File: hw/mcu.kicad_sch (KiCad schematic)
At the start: 22 parts, among them J301 SWD/JTAG, Q301 60V logic-level N-ch, U301 S32K148_144LQFP, U302 TPS3850G33

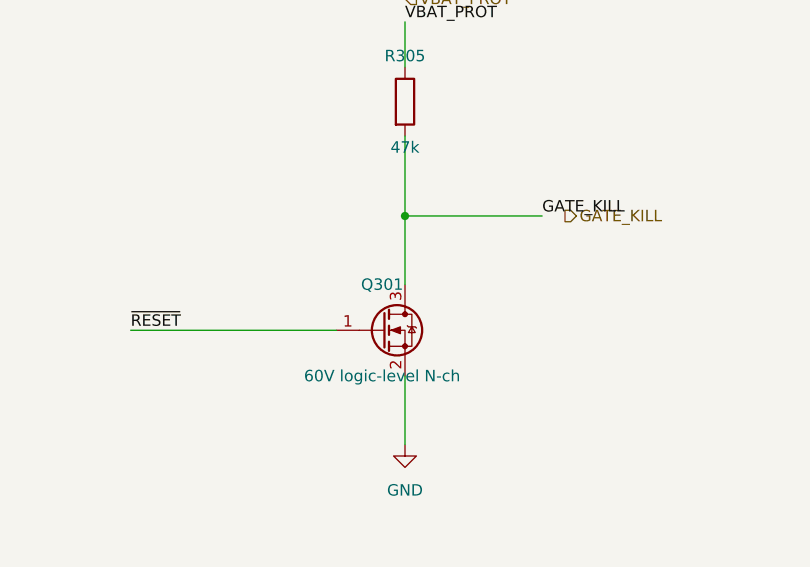
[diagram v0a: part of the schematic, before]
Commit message: Clamp GATE_KILL at 12 V and buffer the relay gates to 5 V
Choosing the small-signal FETs found two gate-drive errors.

GATE_KILL is pulled to VBAT_PROT so the kill path survives a 3V3
brownout, but only FET gates load it, so it followed the rail to
73.3 V on pulse 2a -- 3.7x a +/-20 V Vgs rating. A BZX84-C12-Q now
holds it at 12.7 V (13.7 V hot); transient_clamp checks the margin,
the zener current and the pullup dissipation.

The relay FETs were driven straight from 3.3 V GPIOs, with a note
claiming full enhancement at 3.0 V. No 100 V automotive small-signal
FET checked (PMV280ENEA, DMN10H220LQ, BSS123N) is specified below
Vgs = 4.5 V. An SN74AHCT1G125-Q1 on 5V_MAIN now drives each gate,
with a 100k input pulldown for reset; relay_driver checks overdrive
and drop.

Parts: 2N7002BK for the nine kill FETs and the reset inverter,
PMV280ENEA for the relay FETs. Also fixes the diagonal VBAT_PROT wire
to both relay flyback diodes.

24/24 sim blocks, netlist gate passing, 43 of 297 parts with footprints.
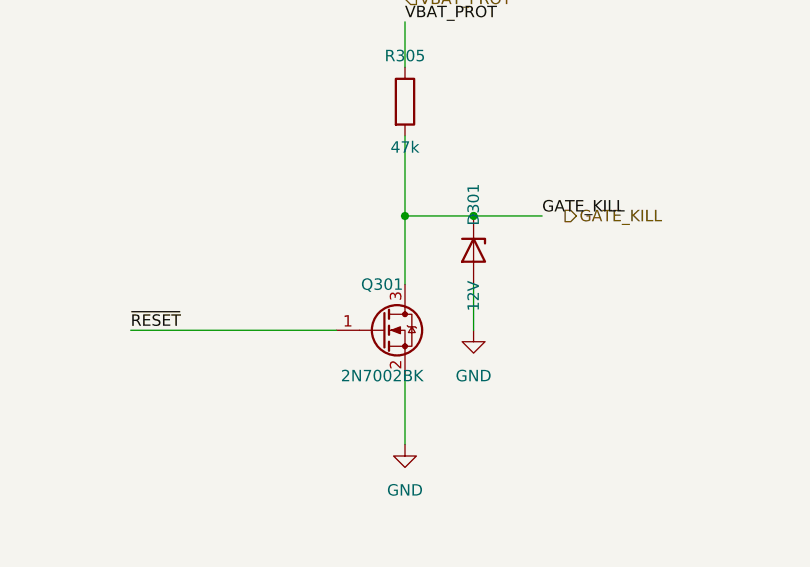
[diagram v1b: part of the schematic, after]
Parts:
- added D301: 12V, Package_TO_SOT_SMD:SOT-23, symbol Device:D_Zener
- Q301: value 60V logic-level N-ch -> 2N7002BK; footprint (none) -> Package_TO_SOT_SMD:SOT-23; MPN (none) -> 2N7002BK; Vgs (none) -> Gate from ~RESET at 3.3 V: Vth 1.1-2.1 V, and it sinks 1.6 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
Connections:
- net GATE_KILL: now also D301.1 (K)
- net GND: now also D301.2 (A)
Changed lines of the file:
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@@
       (effects (font (size 1.27 1.27)))
     )
-    (property "Value" "60V logic-level N-ch" (id 1) (at 295 345.08 0)
-      (effects (font (size 1.27 1.27)))
-    )
-    (property "Footprint" "" (id 2) (at 295 340 0)
+    (property "Value" "2N7002BK" (id 1) (at 295 345.08 0)
+      (effects (font (size 1.27 1.27)))
+    )
+    (property "Footprint" "Package_TO_SOT_SMD:SOT-23" (id 2) (at 295 340 0)
       (effects (font (size 1.27 1.27)) hide)
     )
@@
       (effects (font (size 1.27 1.27)) hide)
     )
-    (property "Source" "memo 11 Recommendation -- 'through one inverting stage'; supervisor.cir models the inverter and kill FET as one switch" (id 4) (at 295 340 0)
-      (effects (font (size 1.27 1.27)) hide)
-    )
-    (property "Note" "RESET low (fault) turns this OFF, so the pullup asserts GATE_KILL high" (id 5) (at 295 340 0)
+    (property "MPN" "2N7002BK" (id 4) (at 295 340 0)
+      (effects (font (size 1.27 1.27)) hide)
+    )
+    (property "Vgs" "Gate from ~RESET at 3.3 V: Vth 1.1-2.1 V, and it sinks 1.6 mA at most (73.3 V / 47k)" (id 5) (at 295 340 0)
+      (effects (font (size 1.27 1.27)) hide)
+    )
+    (property "Source" "memo 11 Recommendation -- 'through one inverting stage'; supervisor.cir models the inverter and kill FET as one switch" (id 6) (at 295 340 0)
+      (effects (font (size 1.27 1.27)) hide)
+    )
+    (property "Note" "RESET low (fault) turns this OFF, so the pullup asserts GATE_KILL high" (id 7) (at 295 340 0)
       (effects (font (size 1.27 1.27)) hide)
     )
@@
     (stroke (width 0) (type default))
   )
-  (wire (pts (xy 297.54 327.3) (xy 312.78 327.3))
-    (stroke (width 0) (type default))
+  (symbol (lib_id "Device:D_Zener") (at 305.16 331.11 270) (unit 1)
+    (in_bom yes) (on_board yes) (fields_autoplaced)
+    (property "Reference" "D301" (id 0) (at 305.16 326.03000000000003 0)
+      (effects (font (size 1.27 1.27)))
+    )
+    (property "Value" "12V" (id 1) (at 305.16 336.19 0)
+      (effects (font (size 1.27 1.27)))
+    )
+    (property "Footprint" "Package_TO_SOT_SMD:SOT-23" (id 2) (at 305.16 331.11 0)
+      (effects (font (size 1.27 1.27)) hide)
+    )
+    (property "Datasheet" "~" (id 3) (at 305.16 331.11 0)
+      (effects (font (size 1.27 1.27)) hide)
+    )
+    (property "MPN" "BZX84-C12-Q" (id 4) (at 305.16 331.11 0)
+      (effects (font (size 1.27 1.27)) hide)
+    )
+    (property "Source" "run_sim transient_clamp -- GATE_KILL clamp" (id 5) (at 305.16 331.11 0)
+      (effects (font (size 1.27 1.27)) hide)
+    )
+    (property "Note" "Cathode GATE_KILL, anode GND: kill gates never exceed 12.7 V against a 20 V Vgs rating, whatever VBAT_PROT does" (id 6) (at 305.16 331.11 0)
+      (effects (font (size 1.27 1.27)) hide)
+    )
+  )
+  (wire (pts (xy 297.54 327.3) (xy 305.16 327.3))
+    (stroke (width 0) (type default))
+  )
+  (wire (pts (xy 305.16 327.3) (xy 312.78 327.3))
+    (stroke (width 0) (type default))
+  )
+  (junction (at 305.16 327.3) (diameter 0) (color 0 0 0 0)
+  )
+  (wire (pts (xy 305.16 334.92) (xy 305.16 340.0))
+    (stroke (width 0) (type default))
+  )
+  (symbol (lib_id "power:GND") (at 305.16 340.0 0) (unit 1)
+    (in_bom yes) (on_board yes) (fields_autoplaced)
+    (property "Reference" "#PWR307" (id 0) (at 305.16 334.92 0)
+      (effects (font (size 1.27 1.27)) hide)
+    )
+    (property "Value" "GND" (id 1) (at 305.16 345.08 0)
+      (effects (font (size 1.27 1.27)))
+    )
+    (property "Footprint" "" (id 2) (at 305.16 340.0 0)
+      (effects (font (size 1.27 1.27)) hide)
+    )
+    (property "Datasheet" "~" (id 3) (at 305.16 340.0 0)
+      (effects (font (size 1.27 1.27)) hide)
+    )
   )
   (label "GATE_KILL" (at 312.78 327.3 0)
@@
   (symbol (lib_id "power:GND") (at 400.0 405.16 0) (unit 1)
     (in_bom yes) (on_board yes) (fields_autoplaced)
-    (property "Reference" "#PWR307" (id 0) (at 400.0 400.08000000000004 0)
+    (property "Reference" "#PWR308" (id 0) (at 400.0 400.08000000000004 0)
       (effects (font (size 1.27 1.27)) hide)
     )
@@
   (symbol (lib_id "power:GND") (at 267.92 405.16 0) (unit 1)
     (in_bom yes) (on_board yes) (fields_autoplaced)
-    (property "Reference" "#PWR308" (id 0) (at 267.92 400.08000000000004 0)
+    (property "Reference" "#PWR309" (id 0) (at 267.92 400.08000000000004 0)
       (effects (font (size 1.27 1.27)) hide)
     )
@@
   (symbol (lib_id "power:GND") (at 385.0 368.1 0) (unit 1)
     (in_bom yes) (on_board yes) (fields_autoplaced)
-    (property "Reference" "#PWR309" (id 0) (at 385 363.02000000000004 0)
-      (effects (font (size 1.27 1.27)) hide)
-    )
+    (property "Reference" "#PWR310" (id 0) (at 385 363.02000000000004 0)
+      (effects (font (size 1.27 1.27)) hide)
+    )

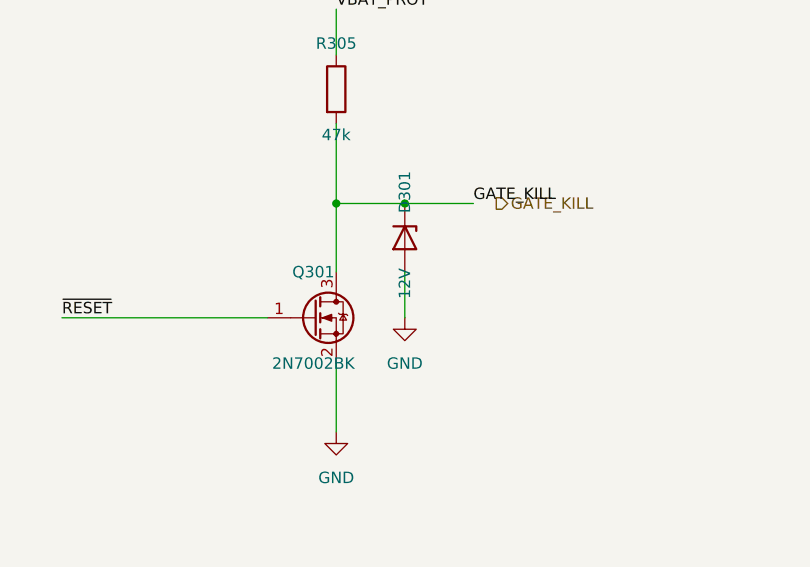
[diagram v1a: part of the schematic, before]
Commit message: Choose the diodes; the boost VDD clamp was 10 V over its pin rating
Part numbers for 27 diodes, each against a retrieved datasheet, applied
through one table (schlib.CHOSEN) keyed by symbol and class value, so
the class stays on the part as a field:
  VS-16EDH02HM3 x7   injector recirculation / blocking / freewheel
  VS-2EMH02HM3       boost diode
  VS-1EMH02HM3 x8    bootstrap and relay flyback
  VS-3ECH02HM3       metering freewheel
  SS20PH102HM3       negative-clamp backstop Schottky
  SMCJ43CA-HM3, SMAJ48CA-HE3, BZX84-C12-Q x2, BZX84-C13-Q, BZG03C36-HM3

The TPS40210 VDD clamp had been checked as an ideal 43.0 V source
behind 47 ohm. The real part in that class (40-46 V, +0.12 %/K, 45 ohm)
puts 61.9 V on a 52 V pin at 125 C, and its 40 V minimum conducts on
the load dump it was chosen to avoid. Now 220 ohm -- which the chosen
switch's gate charge allows -- and a 36 V zener: 46.6 V worst case with
tolerance, tempco and impedance, 33 mA on the dump. 39 V was tried
first; the transient_clamp rail table rejected it at 1.05x. The old
design stays as a pinned check.

TO-277A and SOT-23 zeners put the cathode on pad 3. gen_footprints.py
derives renumbered copies into lib/ecu25kva.pretty (new fp-lib-table).
The GATE_KILL zener, footprinted in the previous commit with the stock
SOT-23, had been reversed.

Left open as LOWV-CLAMP: the 15 zeners at 3.0 and 3.3 V. At tens of uA
a sub-5 V zener's knee is soft -- the datasheet allows 10 uA at 1 V --
and the model's sharp-knee zener hides it.

24/24 sim blocks, netlist gate passing, 74 of 297 parts with footprints.
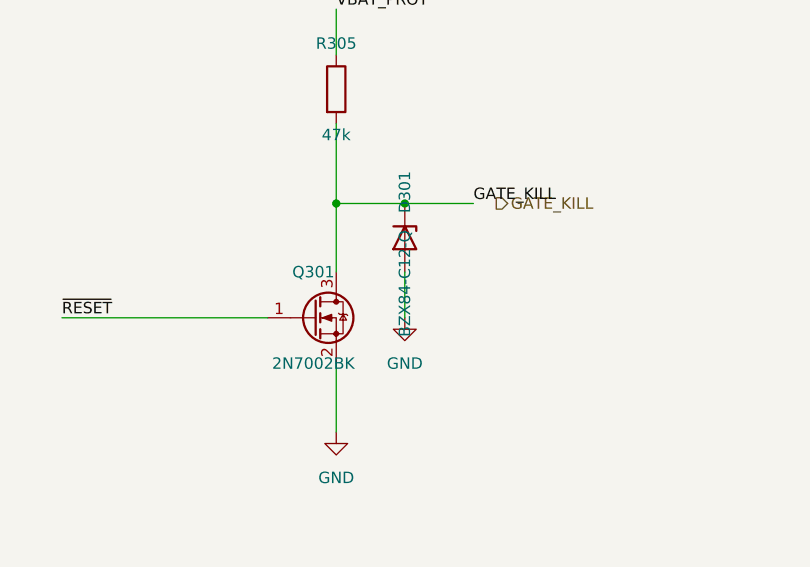
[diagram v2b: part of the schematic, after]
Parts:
- D301: value 12V -> BZX84-C12-Q; footprint Package_TO_SOT_SMD:SOT-23 -> ecu25kva:SOT-23_Zener_K1_A2; Chosen (none) -> Nexperia BZX84-Q, 11.4-12.7 V at 5 mA, AEC-Q101; Class (none) -> 12V
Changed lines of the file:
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@@
       (effects (font (size 1.27 1.27)))
     )
-    (property "Value" "12V" (id 1) (at 305.16 336.19 0)
+    (property "Value" "BZX84-C12-Q" (id 1) (at 305.16 336.19 0)
       (effects (font (size 1.27 1.27)))
     )
-    (property "Footprint" "Package_TO_SOT_SMD:SOT-23" (id 2) (at 305.16 331.11 0)
+    (property "Footprint" "ecu25kva:SOT-23_Zener_K1_A2" (id 2) (at 305.16 331.11 0)
       (effects (font (size 1.27 1.27)) hide)
     )
@@
       (effects (font (size 1.27 1.27)) hide)
     )
-    (property "Source" "run_sim transient_clamp -- GATE_KILL clamp" (id 5) (at 305.16 331.11 0)
+    (property "Class" "12V" (id 5) (at 305.16 331.11 0)
       (effects (font (size 1.27 1.27)) hide)
     )
-    (property "Note" "Cathode GATE_KILL, anode GND: kill gates never exceed 12.7 V against a 20 V Vgs rating, whatever VBAT_PROT does" (id 6) (at 305.16 331.11 0)
+    (property "Chosen" "Nexperia BZX84-Q, 11.4-12.7 V at 5 mA, AEC-Q101" (id 6) (at 305.16 331.11 0)
       (effects (font (size 1.27 1.27)) hide)
     )
+    (property "Source" "run_sim transient_clamp -- GATE_KILL clamp" (id 7) (at 305.16 331.11 0)
+      (effects (font (size 1.27 1.27)) hide)
+    )
+    (property "Note" "Cathode GATE_KILL, anode GND: kill gates never exceed 12.7 V against a 20 V Vgs rating, whatever VBAT_PROT does" (id 8) (at 305.16 331.11 0)
+      (effects (font (size 1.27 1.27)) hide)
+    )

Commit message: Package every resistor and capacitor from the voltage across it
hw/assign_passives.py sizes all 188 chip R and C from a per-net table
of continuous and peak voltage (73.3 V pulse 2a, 104 V boost, bootstrap
domains riding on the bank nodes), against Vishay CRCW e3 resistor
ratings (Umax with 1.09x margin, power derated to 0.588x at a 105 C
board) and KEMET's automotive X7R waterfall (parsed by x-coordinate;
the text layout misreads its columns). schlib.place() applies the map
by ref and value; check_netlist fails on any unpackaged R or C.

Found along the way:
- 4.7 uF at 100 V is not in automotive X7R. The EMI filter C1, buck
  input and boost input are now 2 x 2.2 uF 100 V 1210; emi_filter.cir
  models the pair and its cold corner was re-pinned (0.6 dB worse).
- The twelve 470 ohm gate pulldowns need 2010: 0.31 W each at 100%
  duty. Recorded; 1k may now be possible against the real Crss.
- Local labels at 180 degrees were justified in the wrong frame on
  every sheet -- the bug fixed for hierarchical labels earlier -- so
  their text sat across their own wire. Fixed in schlib.label().

Internal nodes whose voltage matters now carry names (FB_BOOST_MID,
CAN1_SPLIT, ...); auto-names like Net-(R407-Pad2) move when parts are
added ahead of them.

24/24 sim blocks, netlist gate passing, 264 of 302 parts footprinted.
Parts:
- C301, C302, C303, C304, C305, C306, C307, C308, C309, C310, C311, C312: footprint (none) -> Capacitor_SMD:C_0603_1608Metric
- R301, R302, R303, R304: footprint (none) -> Resistor_SMD:R_0603_1608Metric
- R305: footprint (none) -> Resistor_SMD:R_0805_2012Metric
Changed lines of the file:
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@@
   )
   (label "~{RESET}" (at 41.66 75.46 180)
-    (effects (font (size 1.27 1.27)) (justify left bottom))
+    (effects (font (size 1.27 1.27)) (justify right bottom))
   )
   (wire (pts (xy 64.52 72.92) (xy 41.66 72.92))
@@
   )
   (label "JTAG_TMS" (at 41.66 72.92 180)
-    (effects (font (size 1.27 1.27)) (justify left bottom))
+    (effects (font (size 1.27 1.27)) (justify right bottom))
   )
   (wire (pts (xy 414.52 72.92) (xy 391.66 72.92))
@@
   )
   (label "JTAG_TCK" (at 391.66 72.92 180)
-    (effects (font (size 1.27 1.27)) (justify left bottom))
+    (effects (font (size 1.27 1.27)) (justify right bottom))
   )
   (wire (pts (xy 414.52 75.46) (xy 391.66 75.46))
@@
   )
   (label "JTAG_TDI" (at 391.66 75.46 180)
-    (effects (font (size 1.27 1.27)) (justify left bottom))
+    (effects (font (size 1.27 1.27)) (justify right bottom))
   )
   (wire (pts (xy 239.52 218.03) (xy 216.66 218.03))
@@
   )
   (label "WDT_KICK" (at 216.66 218.03 180)
-    (effects (font (size 1.27 1.27)) (justify left bottom))
+    (effects (font (size 1.27 1.27)) (justify right bottom))
   )
   (wire (pts (xy 239.52 220.57) (xy 216.66 220.57))
@@
   )
   (label "WDT_FAULT" (at 216.66 220.57 180)
-    (effects (font (size 1.27 1.27)) (justify left bottom))
+    (effects (font (size 1.27 1.27)) (justify right bottom))
   )
   (wire (pts (xy 414.52 223.11) (xy 391.66 223.11))
@@
   )
   (label "3V3_MCU" (at 391.66 223.11 180)
-    (effects (font (size 1.27 1.27)) (justify left bottom))
+    (effects (font (size 1.27 1.27)) (justify right bottom))
   )
   (wire (pts (xy 475.48 223.11) (xy 498.34 223.11))
@@
   )
   (label "3V3_MCU" (at 391.66 240.89 180)
-    (effects (font (size 1.27 1.27)) (justify left bottom))
+    (effects (font (size 1.27 1.27)) (justify right bottom))
   )
   (wire (pts (xy 414.52 225.65) (xy 391.66 225.65))
@@
   )
   (label "3V3_MCU" (at 391.66 225.65 180)
-    (effects (font (size 1.27 1.27)) (justify left bottom))
+    (effects (font (size 1.27 1.27)) (justify right bottom))
   )
   (wire (pts (xy 414.52 228.19) (xy 391.66 228.19))
@@
   )
   (label "3V3_MCU" (at 391.66 228.19 180)
-    (effects (font (size 1.27 1.27)) (justify left bottom))
+    (effects (font (size 1.27 1.27)) (justify right bottom))
   )
   (wire (pts (xy 475.48 225.65) (xy 498.34 225.65))
@@
   )
   (label "3V3_MCU" (at 391.66 230.73 180)
-    (effects (font (size 1.27 1.27)) (justify left bottom))
+    (effects (font (size 1.27 1.27)) (justify right bottom))
   )
   (wire (pts (xy 475.48 233.27) (xy 498.34 233.27))
@@
   )
   (label "3V3_MCU" (at 391.66 233.27 180)
-    (effects (font (size 1.27 1.27)) (justify left bottom))
+    (effects (font (size 1.27 1.27)) (justify right bottom))
   )
   (wire (pts (xy 475.48 235.81) (xy 498.34 235.81))
@@
   )
   (label "3V3_MCU" (at 391.66 235.81 180)
-    (effects (font (size 1.27 1.27)) (justify left bottom))
+    (effects (font (size 1.27 1.27)) (justify right bottom))
   )
   (wire (pts (xy 475.48 238.35) (xy 498.34 238.35))
@@
   )
   (label "3V3_MCU" (at 391.66 238.35 180)
-    (effects (font (size 1.27 1.27)) (justify left bottom))
+    (effects (font (size 1.27 1.27)) (justify right bottom))
   )
   (symbol (lib_id "ecu25kva:TPS3850G33") (at 120.0 345.0 0) (unit 1)
@@
   )
   (label "3V3_MCU" (at 79.36 338.65 180)
-    (effects (font (size 1.27 1.27)) (justify left bottom))
+    (effects (font (size 1.27 1.27)) (justify right bottom))
   )
   (wire (pts (xy 102.22 341.19) (xy 79.36 341.19))
@@
   )
   (label "WDT_KICK" (at 79.36 341.19 180)
-    (effects (font (size 1.27 1.27)) (justify left bottom))
+    (effects (font (size 1.27 1.27)) (justify right bottom))
   )
   (wire (pts (xy 137.78 341.19) (xy 160.64 341.19))
@@
       (effects (font (size 1.27 1.27)))
     )
-    (property "Footprint" "" (id 2) (at 142.86 323.40999999999997 0)
+    (property "Footprint" "Resistor_SMD:R_0603_1608Metric" (id 2) (at 142.86 323.40999999999997 0)
       (effects (font (size 1.27 1.27)) hide)
     )
@@
       (effects (font (size 1.27 1.27)))
     )
-    (property "Footprint" "" (id 2) (at 142.86 325.95 0)
+    (property "Footprint" "Resistor_SMD:R_0603_1608Metric" (id 2) (at 142.86 325.95 0)
       (effects (font (size 1.27 1.27)) hide)
     )
@@
       (effects (font (size 1.27 1.27)))
     )
-    (property "Footprint" "" (id 2) (at 76.82 375.48 0)
+    (property "Footprint" "Capacitor_SMD:C_0603_1608Metric" (id 2) (at 76.82 375.48 0)
       (effects (font (size 1.27 1.27)) hide)
     )
@@
       (effects (font (size 1.27 1.27)))
     )
-    (property "Footprint" "" (id 2) (at 64.12 375.48 0)
+    (property "Footprint" "Capacitor_SMD:C_0603_1608Metric" (id 2) (at 64.12 375.48 0)
       (effects (font (size 1.27 1.27)) hide)
     )
@@
       (effects (font (size 1.27 1.27)))
     )
-    (property "Footprint" "" (id 2) (at 51.42 375.48 0)
+    (property "Footprint" "Resistor_SMD:R_0603_1608Metric" (id 2) (at 51.42 375.48 0)
       (effects (font (size 1.27 1.27)) hide)
     )
@@
       (effects (font (size 1.27 1.27)))
     )
-    (property "Footprint" "" (id 2) (at 38.72 375.48 0)
+    (property "Footprint" "Resistor_SMD:R_0603_1608Metric" (id 2) (at 38.72 375.48 0)
       (effects (font (size 1.27 1.27)) hide)
     )
@@
   )
   (label "~{RESET}" (at 267.06 340.0 180)
-    (effects (font (size 1.27 1.27)) (justify left bottom))
+    (effects (font (size 1.27 1.27)) (justify right bottom))
   )
   (wire (pts (xy 297.54 345.08) (xy 297.54 352.7))
@@
       (effects (font (size 1.27 1.27)))
     )
-    (property "Footprint" "" (id 2) (at 297.54 314.6 0)
+    (property "Footprint" "Resistor_SMD:R_0805_2012Metric" (id 2) (at 297.54 314.6 0)
       (effects (font (size 1.27 1.27)) hide)
     )
@@
       (effects (font (size 1.27 1.27)))
     )
-    (property "Footprint" "" (id 2) (at 400.0 395 0)
+    (property "Footprint" "Capacitor_SMD:C_0603_1608Metric" (id 2) (at 400.0 395 0)
       (effects (font (size 1.27 1.27)) hide)
     )
@@
       (effects (font (size 1.27 1.27)))
     )
-    (property "Footprint" "" (id 2) (at 387.3 395 0)
+    (property "Footprint" "Capacitor_SMD:C_0603_1608Metric" (id 2) (at 387.3 395 0)
       (effects (font (size 1.27 1.27)) hide)
     )
@@
       (effects (font (size 1.27 1.27)))
     )
-    (property "Footprint" "" (id 2) (at 374.6 395 0)
+    (property "Footprint" "Capacitor_SMD:C_0603_1608Metric" (id 2) (at 374.6 395 0)
       (effects (font (size 1.27 1.27)) hide)
     )
@@
       (effects (font (size 1.27 1.27)))
     )
-    (property "Footprint" "" (id 2) (at 361.9 395 0)
+    (property "Footprint" "Capacitor_SMD:C_0603_1608Metric" (id 2) (at 361.9 395 0)
       (effects (font (size 1.27 1.27)) hide)
     )
@@
       (effects (font (size 1.27 1.27)))
     )
-    (property "Footprint" "" (id 2) (at 349.2 395 0)
+    (property "Footprint" "Capacitor_SMD:C_0603_1608Metric" (id 2) (at 349.2 395 0)
       (effects (font (size 1.27 1.27)) hide)
     )
@@
       (effects (font (size 1.27 1.27)))
     )
-    (property "Footprint" "" (id 2) (at 336.5 395 0)
+    (property "Footprint" "Capacitor_SMD:C_0603_1608Metric" (id 2) (at 336.5 395 0)
       (effects (font (size 1.27 1.27)) hide)
     )
@@
       (effects (font (size 1.27 1.27)))
     )
-    (property "Footprint" "" (id 2) (at 323.8 395 0)
+    (property "Footprint" "Capacitor_SMD:C_0603_1608Metric" (id 2) (at 323.8 395 0)
       (effects (font (size 1.27 1.27)) hide)
     )
@@
       (effects (font (size 1.27 1.27)))
     )
-    (property "Footprint" "" (id 2) (at 311.1 395 0)
+    (property "Footprint" "Capacitor_SMD:C_0603_1608Metric" (id 2) (at 311.1 395 0)
       (effects (font (size 1.27 1.27)) hide)
     )
@@
       (effects (font (size 1.27 1.27)))
     )
-    (property "Footprint" "" (id 2) (at 298.4 395 0)
+    (property "Footprint" "Capacitor_SMD:C_0603_1608Metric" (id 2) (at 298.4 395 0)
       (effects (font (size 1.27 1.27)) hide)
     )
@@
       (effects (font (size 1.27 1.27)))
     )
-    (property "Footprint" "" (id 2) (at 285.7 395 0)
-      (effects (font (size 1.27 1.27)) hide)
-    )
+    (property "Footprint" "Capacitor_SMD:C_0603_1608Metric" (id 2) (at 285.7 395 0)
+      (effects (font (size 1.27 1.27)) hide)
+    )
